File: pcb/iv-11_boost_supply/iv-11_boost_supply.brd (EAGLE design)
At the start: 100 x 80 mm, 15 parts, among them IC1 LM555D, M1 IRF540NPBF

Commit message: Did most of the board layout, found more parts to order
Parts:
- added JP2: (no value), SparkFun-Connectors:1X03_LOCK
- added R4: 10k, SparkFun-Passives:1206
- added R6: 110k, SparkFun-Passives:1206
- D2: device adafruit:DO201T15 -> adafruit:DO35-7
- M1: value IRF540NPBF -> IRF540
- moved C3 94.6 mm to (48.3, 6.35)
- moved L1 82.6 mm to (54.6, 29.2), turned to 90 degrees
- moved D2 79.8 mm to (54.6, 15.2), turned to 90 degrees
- moved D3 78.9 mm to (38.1, 5.08), turned to 180 degrees
- moved R3 72.2 mm to (43.2, 15.2), turned to 180 degrees
- moved M1 65.6 mm to (43.2, 27.9)
- moved C1 64.1 mm to (21.6, 33.0), turned to 90 degrees
- moved R1 61.6 mm to (14.0, 33.0), turned to 90 degrees
- moved C2 56.7 mm to (17.8, 40.6), turned to 90 degrees
- moved R5 55.1 mm to (17.8, 26.7), turned to 270 degrees
- moved F1 52.7 mm to (7.62, 32.5), turned to 270 degrees
- moved IC1 48.3 mm to (30.5, 26.7), turned to 90 degrees
- moved JP1 47.7 mm to (5.08, 17.8), turned to 270 degrees
- moved D1 43.3 mm to (17.8, 20.3)
- moved R2 36.9 mm to (17.8, 33.0), turned to 90 degrees
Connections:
- removed net PWM: JP1.3
- removed net V+: IC1.8
- new net 555_CAP: C1.1, D1.C, IC1.2, IC1.6, R2.1
- new net 555_CTL: D1.A, IC1.7, R5.B
- new net 555_PWM: IC1.3, JP2.3
- new net EXT_PWM: JP1.3, JP2.1
- new net N$1: R1.1, R5.A
- new net N$2: R2.2, R5.C
- new net N$4: D2.A, L1.2, M1.2
- new net PWR_PWM: JP2.2, M1.1, R3.2
- new net VCC_PRC: C2.1, F1.P$1, F1.P$2, IC1.4, IC1.8, L1.1, R1.2
- net BST: now also C3.1, D2.C, D3.P$1, R6.1
- net FBK: now also R4.1, R6.2
- net GND: now also C1.2, C2.2, C3.2, D3.P$2, M1.3, R3.1, R4.2
- net VCC: now also F1.P$3, F1.P$4
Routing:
- added copper zone on layer 16, net GND
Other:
- board size 100 x 80 mm -> 61.9 x 49.5 mm

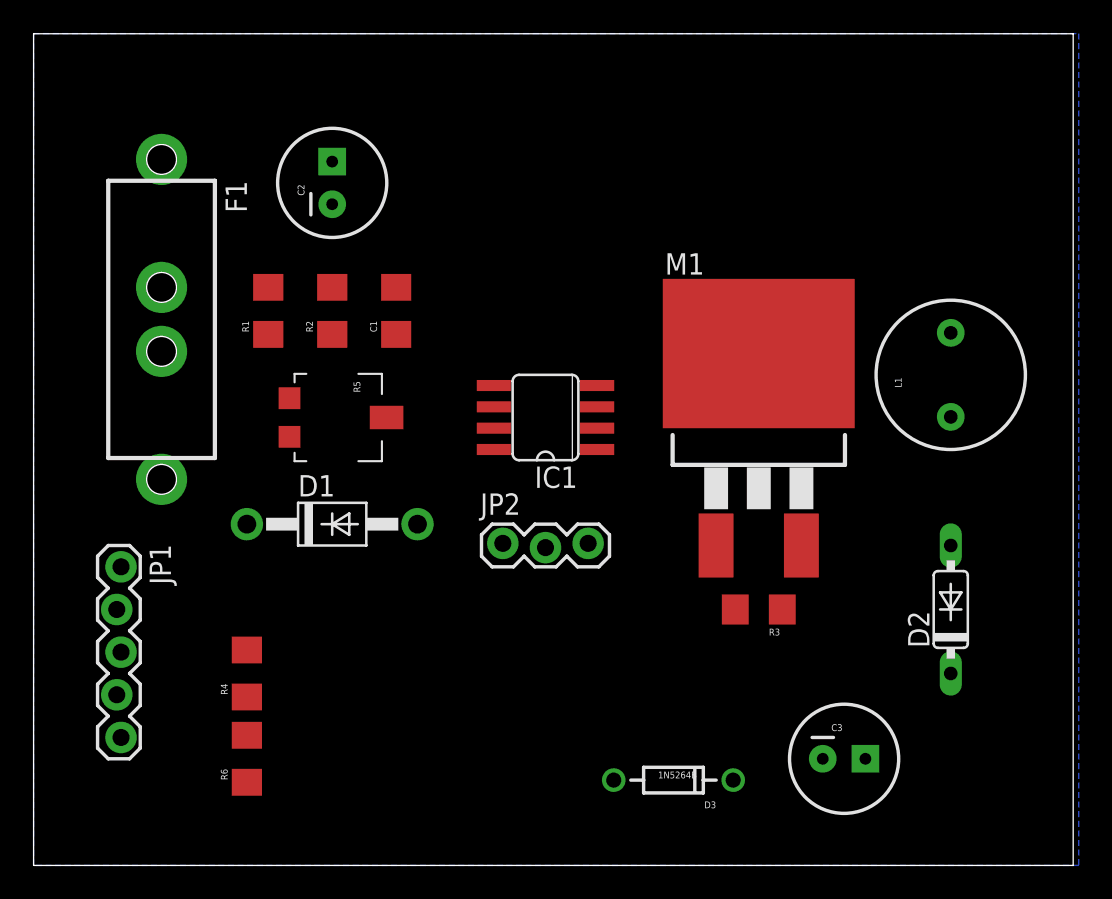
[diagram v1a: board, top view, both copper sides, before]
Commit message: Cleaned up the board layout, need the parts to test it out on paper
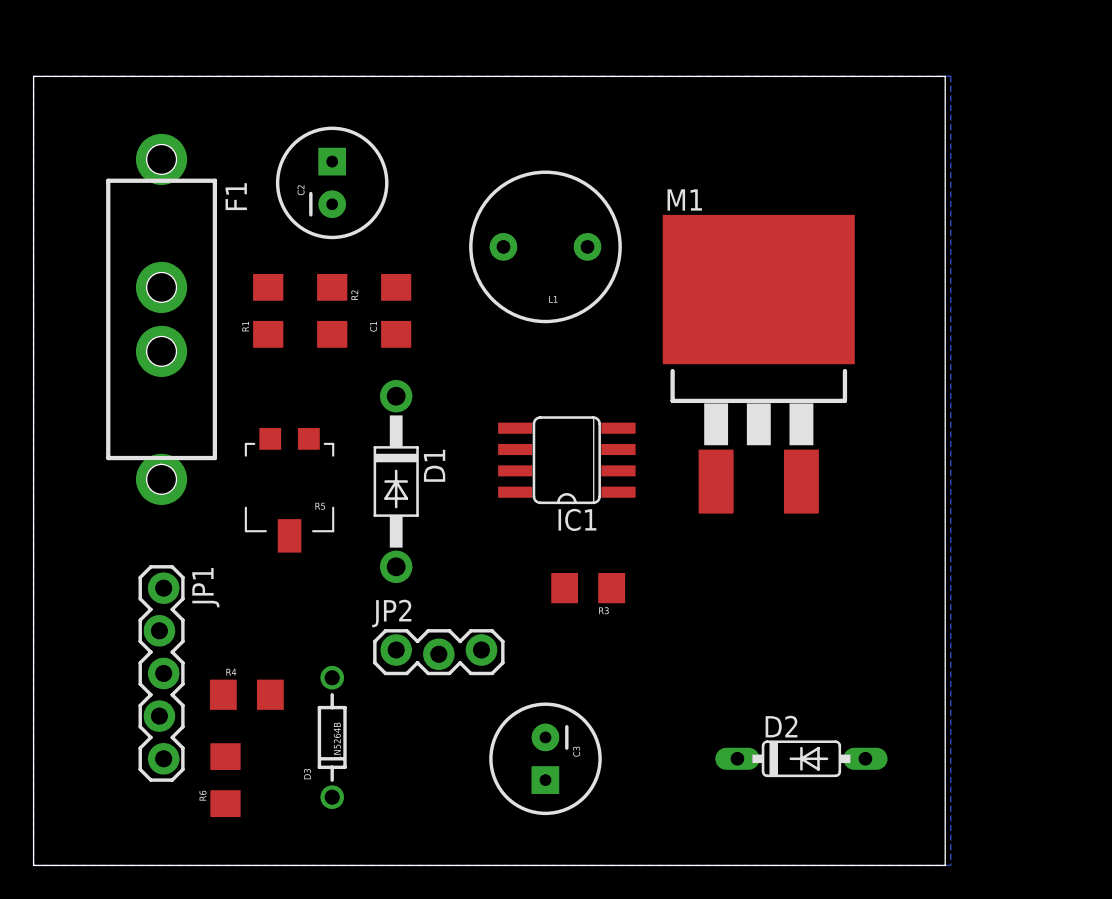
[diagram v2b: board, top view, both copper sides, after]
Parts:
- moved L1 25.3 mm to (30.5, 36.8), turned to 180 degrees
- moved D3 20.5 mm to (17.8, 7.62), turned to 90 degrees
- moved C3 17.8 mm to (30.5, 6.35), turned to 270 degrees
- moved D2 12.6 mm to (45.7, 6.35), turned to 0 degrees
- moved R3 10.2 mm to (33.0, 16.5)
- moved JP2 8.98 mm to (21.6, 12.7)
- moved R5 4.58 mm to (15.2, 22.9), turned to 180 degrees
- moved D1 4.58 mm to (21.6, 22.9), turned to 270 degrees
- moved M1 3.81 mm to (43.2, 31.8)
- moved IC1 2.84 mm to (31.8, 24.1)
- moved JP1 2.84 mm to (7.62, 16.5)
- moved R6 1.80 mm to (11.4, 5.08)
- moved R4 1.27 mm to (12.7, 10.2), turned to 0 degrees
- turned R2 to 270 degrees
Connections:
- net EXT_PWM: now also JP1.2; no longer JP1.3
- net GND: now also JP1.3; no longer JP1.2
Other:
- board size 61.9 x 49.5 mm -> 54.3 x 47 mm

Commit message: Not entirely sure what changed here, but Eagle wanted to save things
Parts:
- moved JP2 4.58 mm to (25.4, 15.2)
- moved C3 2.84 mm to (27.9, 7.62)
- moved D2 2.54 mm to (43.2, 6.35)
- moved R3 2.54 mm to (35.6, 16.5), turned to 90 degrees
- moved R6 1.80 mm to (12.7, 6.35)
- moved M1 1.27 mm to (43.2, 33.0)
- moved IC1 1.27 mm to (30.5, 24.1)
- moved R4 1.27 mm to (12.7, 11.4)
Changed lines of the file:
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@@
 <element name="C1" library="SparkFun-Passives" package="1206" value="10nF" x="21.59" y="33.02" rot="R90"/>
 <element name="C2" library="SparkFun-Passives" package="CPOL-RADIAL-100UF-25V" value="47uF" x="17.78" y="40.64" rot="R90"/>
-<element name="C3" library="SparkFun-Passives" package="CPOL-RADIAL-100UF-25V" value="100uF" x="30.48" y="6.35" rot="R270"/>
+<element name="C3" library="SparkFun-Passives" package="CPOL-RADIAL-100UF-25V" value="100uF" x="27.94" y="7.62" rot="R270"/>
 <element name="D1" library="adafruit" package="DO41-10" value="1N4004" x="21.59" y="22.86" rot="R270"/>
 <element name="D3" library="SparkFun-DiscreteSemi" package="DIODE-ZENER" value="1N5264B" x="17.78" y="7.62" rot="R90"/>
 <element name="F1" library="boztalay" package="1AG-1/4X5/8-FUSE" value="2A/32V" x="7.62" y="32.512" rot="R270"/>
-<element name="IC1" library="adafruit" package="SO08" value="LM555D" x="31.75" y="24.13" rot="R90"/>
+<element name="IC1" library="adafruit" package="SO08" value="LM555D" x="30.48" y="24.13" rot="R90"/>
 <element name="JP1" library="SparkFun-Connectors" package="1X05_LOCK" value="" x="7.62" y="16.51" rot="R270"/>
-<element name="JP2" library="SparkFun-Connectors" package="1X03_LOCK" value="" x="21.59" y="12.7"/>
+<element name="JP2" library="SparkFun-Connectors" package="1X03_LOCK" value="" x="25.4" y="15.24"/>
 <element name="L1" library="SparkFun-Passives" package="RLB0912" value="2200uH" x="30.48" y="36.83" rot="R180"/>
-<element name="M1" library="boztalay" package="D2PACK" value="IRF540" x="43.18" y="31.75"/>
+<element name="M1" library="boztalay" package="D2PACK" value="IRF540" x="43.18" y="33.02"/>
 <element name="R1" library="SparkFun-Passives" package="1206" value="100" x="13.97" y="33.02" rot="R90"/>
 <element name="R2" library="SparkFun-Passives" package="1206" value="100" x="17.78" y="33.02" rot="R270"/>
-<element name="R3" library="SparkFun-Passives" package="1206" value="10k" x="33.02" y="16.51" rot="R180"/>
-<element name="R4" library="SparkFun-Passives" package="1206" value="10k" x="12.7" y="10.16"/>
+<element name="R3" library="SparkFun-Passives" package="1206" value="10k" x="35.56" y="16.51" rot="R90"/>
+<element name="R4" library="SparkFun-Passives" package="1206" value="10k" x="12.7" y="11.43"/>
 <element name="R5" library="SparkFun-Electromechanical" package="TRIMPOT-5MM-V2" value="10k" x="15.24" y="22.86" rot="R180"/>
-<element name="R6" library="SparkFun-Passives" package="1206" value="110k" x="11.43" y="5.08" rot="R90"/>
-<element name="D2" library="adafruit" package="DO35-7" value="MBR160" x="45.72" y="6.35"/>
+<element name="R6" library="SparkFun-Passives" package="1206" value="110k" x="12.7" y="6.35" rot="R90"/>
+<element name="D2" library="adafruit" package="DO35-7" value="MBR160" x="43.18" y="6.35"/>
 </elements>
 <signals>
@@
 </polygon>
 <contactref element="JP1" pad="3"/>
-<wire x1="34.8234" y1="22.225" x2="45.72" y2="22.86" width="0" layer="19" extent="1-1"/>
-<wire x1="34.42" y1="16.51" x2="34.8234" y2="22.225" width="0" layer="19" extent="1-1"/>
-<wire x1="30.48" y1="7.62" x2="34.42" y2="16.51" width="0" layer="19" extent="1-1"/>
-<wire x1="14.1" y1="10.16" x2="17.78" y2="11.176" width="0" layer="19" extent="1-1"/>
+<via x="44.45" y="20.32" extent="1-16" drill="0.508" diameter="1.27"/>
+<via x="46.99" y="20.32" extent="1-16" drill="0.508" diameter="1.27"/>
+<via x="34.29" y="20.32" extent="1-16" drill="0.508"/>
+<wire x1="44.45" y1="20.32" x2="45.72" y2="24.13" width="0" layer="19" extent="1-1"/>
+<wire x1="33.5534" y1="22.225" x2="34.29" y2="20.32" width="0" layer="19" extent="1-1"/>
+<wire x1="14.1" y1="11.43" x2="17.78" y2="11.176" width="0" layer="19" extent="1-1"/>
+<wire x1="35.56" y1="15.11" x2="34.29" y2="20.32" width="0" layer="19" extent="1-1"/>
 <wire x1="21.59" y1="34.42" x2="17.78" y2="39.37" width="0" layer="19" extent="1-1"/>
 </signal>
@@
 <contactref element="R6" pad="2"/>
 <contactref element="R4" pad="1"/>
-<wire x1="11.43" y1="6.48" x2="11.3" y2="10.16" width="0" layer="19" extent="1-1"/>
-<wire x1="7.493" y1="8.89" x2="11.3" y2="10.16" width="0" layer="19" extent="1-1"/>
+<wire x1="11.3" y1="11.43" x2="12.7" y2="7.75" width="0" layer="19" extent="1-1"/>
+<wire x1="7.493" y1="8.89" x2="11.3" y2="11.43" width="0" layer="19" extent="1-1"/>
 </signal>
 <signal name="BST">
@@
 <contactref element="D2" pad="C"/>
 <contactref element="R6" pad="1"/>
-<wire x1="30.48" y1="5.08" x2="41.91" y2="6.35" width="0" layer="19" extent="1-1"/>
-<wire x1="17.78" y1="4.064" x2="30.48" y2="5.08" width="0" layer="19" extent="1-1"/>
-<wire x1="11.43" y1="3.68" x2="17.78" y2="4.064" width="0" layer="19" extent="1-1"/>
-<wire x1="7.747" y1="6.35" x2="11.43" y2="3.68" width="0" layer="19" extent="1-1"/>
+<wire x1="27.94" y1="6.35" x2="39.37" y2="6.35" width="0" layer="19" extent="1-1"/>
+<wire x1="17.78" y1="4.064" x2="27.94" y2="6.35" width="0" layer="19" extent="1-1"/>
+<wire x1="12.7" y1="4.95" x2="17.78" y2="4.064" width="0" layer="19" extent="1-1"/>
+<wire x1="7.747" y1="6.35" x2="12.7" y2="4.95" width="0" layer="19" extent="1-1"/>
 </signal>
 <signal name="N$1">
@@
 <contactref element="IC1" pad="7"/>
 <contactref element="D1" pad="A"/>
-<wire x1="21.59" y1="17.78" x2="28.6766" y2="23.495" width="0" layer="19" extent="1-1"/>
+<wire x1="21.59" y1="17.78" x2="27.4066" y2="23.495" width="0" layer="19" extent="1-1"/>
 <wire x1="15.24" y1="19.6215" x2="21.59" y2="17.78" width="0" layer="19" extent="1-1"/>
 </signal>
@@
 <contactref element="IC1" pad="6"/>
 <contactref element="IC1" pad="2"/>
-<wire x1="28.6766" y1="24.765" x2="34.8234" y2="23.495" width="0" layer="19" extent="1-1"/>
-<wire x1="21.59" y1="27.94" x2="28.6766" y2="24.765" width="0" layer="19" extent="1-1"/>
+<wire x1="27.4066" y1="24.765" x2="33.5534" y2="23.495" width="0" layer="19" extent="1-1"/>
+<wire x1="21.59" y1="27.94" x2="27.4066" y2="24.765" width="0" layer="19" extent="1-1"/>
 <wire x1="21.59" y1="31.62" x2="21.59" y2="27.94" width="0" layer="19" extent="1-1"/>
 <wire x1="17.78" y1="34.42" x2="21.59" y2="31.62" width="0" layer="19" extent="1-1"/>
@@
 <contactref element="IC1" pad="3"/>
 <contactref element="JP2" pad="3"/>
-<wire x1="26.67" y1="12.827" x2="34.8234" y2="24.765" width="0" layer="19" extent="1-1"/>
+<wire x1="30.48" y1="15.367" x2="33.5534" y2="24.765" width="0" layer="19" extent="1-1"/>
 </signal>
 <signal name="PWR_PWM">
@@
 <contactref element="M1" pad="1"/>
 <contactref element="R3" pad="2"/>
-<wire x1="31.62" y1="16.51" x2="40.64" y2="22.86" width="0" layer="19" extent="1-1"/>
-<wire x1="24.13" y1="12.573" x2="31.62" y2="16.51" width="0" layer="19" extent="1-1"/>
+<wire x1="35.56" y1="17.91" x2="40.64" y2="24.13" width="0" layer="19" extent="1-1"/>
+<wire x1="27.94" y1="15.113" x2="35.56" y2="17.91" width="0" layer="19" extent="1-1"/>
 </signal>
 <signal name="EXT_PWM">
 <contactref element="JP2" pad="1"/>
 <contactref element="JP1" pad="2"/>
-<wire x1="7.493" y1="13.97" x2="21.59" y2="12.827" width="0" layer="19" extent="1-1"/>
+<wire x1="7.493" y1="13.97" x2="25.4" y2="15.367" width="0" layer="19" extent="1-1"/>
 </signal>
 <signal name="N$4">
@@
 <contactref element="M1" pad="2"/>
 <contactref element="D2" pad="A"/>
-<wire x1="32.9819" y1="36.83" x2="43.18" y2="34.29" width="0" layer="19" extent="1-1"/>
-<wire x1="49.53" y1="6.35" x2="43.18" y2="34.29" width="0" layer="19" extent="1-1"/>
+<wire x1="32.9819" y1="36.83" x2="43.18" y2="35.56" width="0" layer="19" extent="1-1"/>
+<wire x1="46.99" y1="6.35" x2="43.18" y2="35.56" width="0" layer="19" extent="1-1"/>
 </signal>
 <signal name="VCC_PRC">
@@
 <wire x1="7.62" y1="34.417" x2="13.97" y2="34.42" width="0" layer="19" extent="1-1"/>
 <wire x1="7.62" y1="42.037" x2="7.62" y2="34.417" width="0" layer="19" extent="1-1"/>
-<wire x1="34.8234" y1="26.035" x2="27.9781" y2="36.83" width="0" layer="19" extent="1-1"/>
-<wire x1="28.6766" y1="22.225" x2="34.8234" y2="26.035" width="0" layer="19" extent="1-1"/>
+<wire x1="33.5534" y1="26.035" x2="27.9781" y2="36.83" width="0" layer="19" extent="1-1"/>
+<wire x1="27.4066" y1="22.225" x2="33.5534" y2="26.035" width="0" layer="19" extent="1-1"/>
 </signal>
 </signals>

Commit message: Finalizing the layout
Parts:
- moved C3 5.24 mm to (22.9, 6.35)
- moved D2 5.24 mm to (41.9, 11.4), turned to 45 degrees
- moved M1 2.84 mm to (44.5, 30.5), turned to 180 degrees
- moved D3 1.27 mm to (16.5, 7.62)
- moved JP2 1.27 mm to (25.4, 14.0)
- moved R6 1.27 mm to (11.4, 6.35)
- moved L1 1.27 mm to (30.5, 35.6)
- turned R3 to 270 degrees
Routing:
- added copper zone on layer 16, net N$3
- removed copper zone on layer 16, net GND
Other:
- board size 54.3 x 47 mm -> 54.6 x 47 mm

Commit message: First draft of routing
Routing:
- net PWR_PWM: track 0.00 -> 61.3 mm, vias 0 -> 1
- net VCC_PRC: track 0.00 -> 60.0 mm
- net BST: track 0.00 -> 34.6 mm
- net N$4: track 0.00 -> 30.0 mm
- net 555_CAP: track 0.00 -> 26.1 mm, vias 0 -> 2
- net GND: track 0.00 -> 24.1 mm
- net EXT_PWM: track 0.00 -> 18.0 mm
- net 555_CTL: track 0.00 -> 16.7 mm
- net 555_PWM: track 0.00 -> 14.8 mm, vias 0 -> 1
- net VCC: track 0.00 -> 14.2 mm
- net FBK: track 0.00 -> 8.12 mm
- net N$2: track 0.00 -> 6.80 mm
- net N$1: track 0.00 -> 6.27 mm
- added copper zone on layer 16, net GND
- removed copper zone on layer 16, net N$3
